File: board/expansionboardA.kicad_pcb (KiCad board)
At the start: 2 copper layers, 131 x 83.8 mm, 73 parts, among them J2 USB_A_Stacked, J3 HDMI_A, J4 USB_C_Receptacle, SW1 ESPPROG, U2 GPIO_U2, U3 SII164CTG64, U4 GPIO_U4, U5 ESP32-C6-WROOM-1-N8, U6 CS4344-CZZR, U7 MAX3421EEHJ+T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

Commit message: board update
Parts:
- added C3: 0.1uf, Capacitor_SMD:C_0603_1608Metric_Pad1.08x0.95mm_HandSolder, B.Cu at (79.5, 110.8)
- added SW2: ESPRESET, Button_Switch_SMD:SW_Tactile_SPST_NO_Straight_CK_PTS636Sx25SMTRLFS, B.Cu at (78.6, 117.3)
- SW1: moved to B.Cu
- moved SW1 0.30 mm to (71.8, 117.3)
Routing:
- net Net-(U5-EN): track 13.3 -> 73.3 mm, vias 0 -> 2
- net Net-(U5-IO9): vias 1 -> 2
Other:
- board text added: "RESET"
- board text removed: "D2"
- board text removed: "K4"
- board text removed: "L1"
- board text removed: "L3"
- board text removed: "M3"

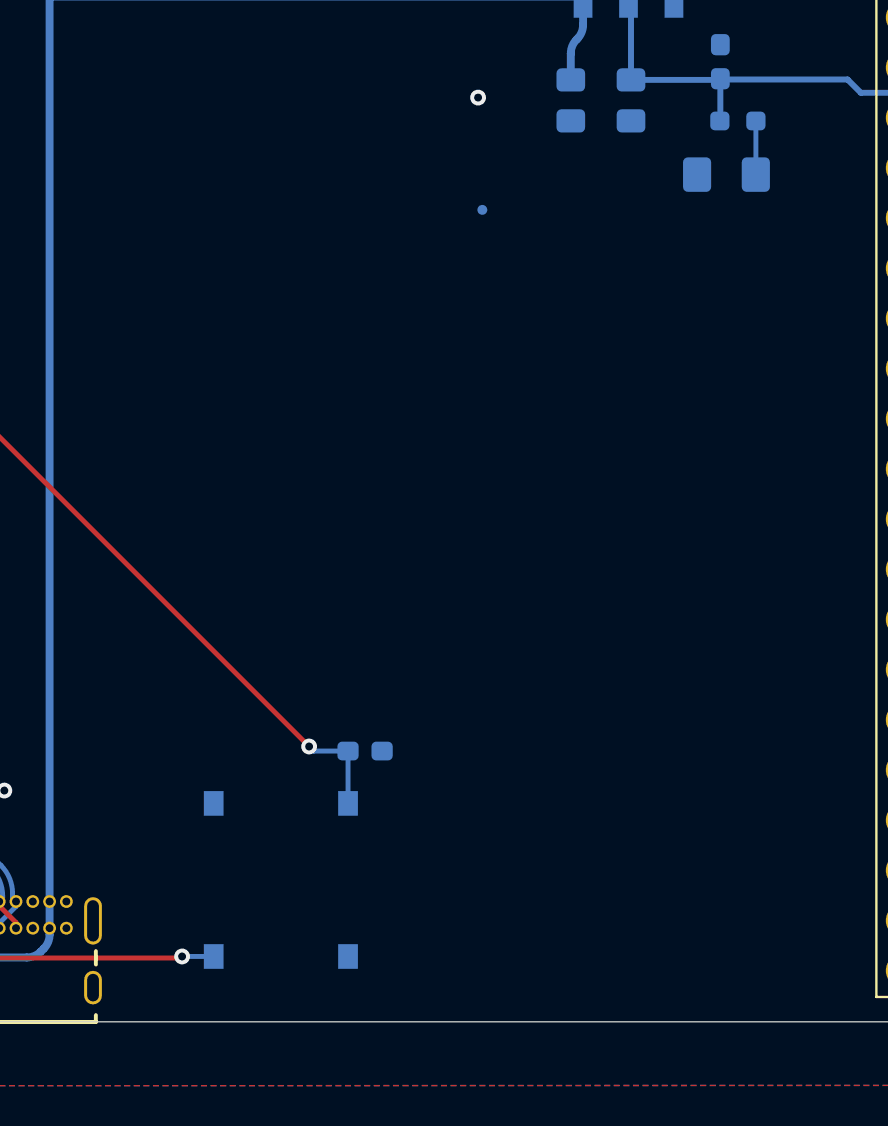
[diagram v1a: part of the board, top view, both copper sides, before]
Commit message: Some reboot/reset work Moved ADC to MIG as internal component Updated ROM startup sequence
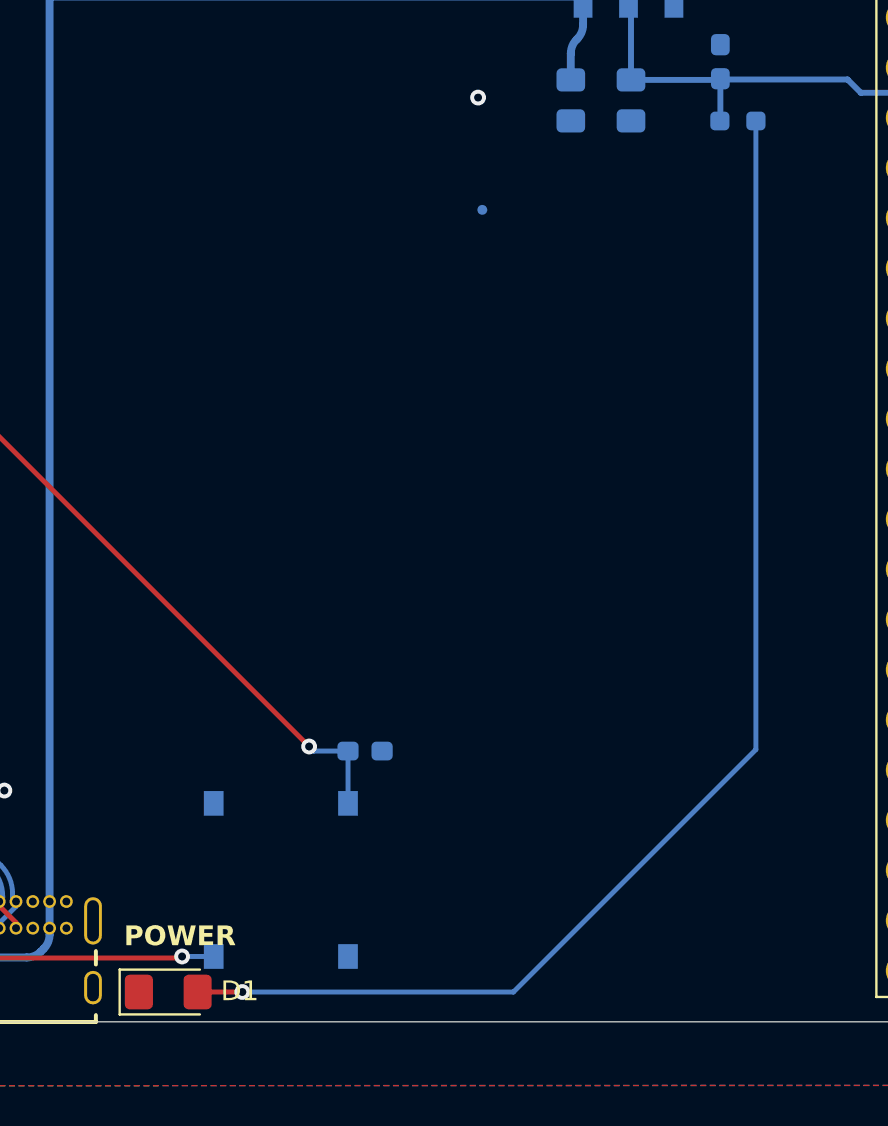
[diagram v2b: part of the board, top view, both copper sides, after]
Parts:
- D1: moved to F.Cu
- moved D1 50.1 mm to (69.5, 123.0)
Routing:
- net Net-(D1-A): track 2.72 -> 65.2 mm, vias 0 -> 1
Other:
- board text added: "ESP32 PROG & UART"
- board text removed: "ESP32 PROG"

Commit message: Board updates for version 2G Factory test ROM update
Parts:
- removed the REF** at (131.8, 96.2)
- removed the REF** at (121.8, 59.8)
- removed the REF** at (87.0, 49.0)
- removed the REF** at (62.2, 62.4)
- removed the REF** at (85.4, 83.4)
- removed the REF** at (148.2, 102.8)
- removed the REF** at (29.5, 66.2)
- removed the REF** at (35.8, 119.8)
- added U1: ESP32-S3, ESP32_S3:QFN56_7X7_EXP-L, B.Cu at (90.9, 104.6)
- moved D1 89.8 mm to (151.2, 85.8), turned to 90 degrees
- moved C3 13.1 mm to (67.2, 115.6), turned to 90 degrees
- moved SW2 5.54 mm to (73.1, 116.5), turned to 180 degrees
- moved SW1 4.14 mm to (73.1, 121.2), turned to 180 degrees
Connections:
- U3 pad 11: unconnected-(U3-MSEN-Pad11) -> MONITORSENSE
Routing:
- net 5V: track 183.8 -> 197.8 mm
- net Net-(D1-A): track 65.2 -> 53.9 mm
- net Net-(U5-IO9): track 41.6 -> 37.0 mm
- net GND: vias 35 -> 36
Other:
- board text added: "PROG UART"
- board text added: "tinysys issue 2G December 2024 Engin Cilasun"
- board text removed: "ESP32 PROG & UART"
- board text removed: "tinysys issue 2F April 2024 Engin Cilasun"

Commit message: New board files for future versions
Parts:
- removed C1: 1uf, Capacitor_SMD:C_0603_1608Metric_Pad1.08x0.95mm_HandSolder
- removed C15, C16: 18pf, Capacitor_SMD:C_0603_1608Metric_Pad1.08x0.95mm_HandSolder
- removed C18, C2, C3: 0.1uf, Capacitor_SMD:C_0603_1608Metric_Pad1.08x0.95mm_HandSolder
- removed C20: 4.7uf, Capacitor_SMD:CP_Elec_4x5.4
- removed J2: USB_A_Stacked, Connector_USB:USB_A_Molex_67643_Horizontal
- removed J4: USB_C_Receptacle, USB4085-GF-A_REVA4:GCT_USB4085-GF-A_REVA4
- removed R16, R17: 33Ohm, Resistor_SMD:R_0603_1608Metric_Pad0.98x0.95mm_HandSolder
- removed R25: 10KOhm, Resistor_SMD:R_0603_1608Metric_Pad0.98x0.95mm_HandSolder
- removed SW1: ESPPROG, Button_Switch_SMD:SW_Tactile_SPST_NO_Straight_CK_PTS636Sx25SMTRLFS
- removed SW2: ESPRESET, Button_Switch_SMD:SW_Tactile_SPST_NO_Straight_CK_PTS636Sx25SMTRLFS
- removed U5: ESP32-C6-WROOM-1-N8, ESP32_C6_WROOM:MOD28_ESP32-C6-WROOM-1_EXP
- removed U7: MAX3421EEHJ+T, MAX3421EEHJ_T:21-0110-C_90-0149-32L_MXM
- removed Y2: 403C35D12M00000, 403C35D12M00000:XTAL_403C35D12M00000
- added C4: 0.1uf, Capacitor_SMD:C_0603_1608Metric_Pad1.08x0.95mm_HandSolder, B.Cu at (75.4, 54.2)
- added C5: 0.1uf, Capacitor_SMD:C_0603_1608Metric_Pad1.08x0.95mm_HandSolder, B.Cu at (75.4, 57.3)
- added J1: USB_C_Receptacle, USB4085-GF-A_REVA4:GCT_USB4085-GF-A_REVA4, F.Cu at (23.8, 89.0)
- added R2: 10KOhm, Resistor_SMD:R_0603_1608Metric_Pad0.98x0.95mm_HandSolder, B.Cu at (75.5, 50.9)
- added SW3: ESPRESET, Button_Switch_SMD:SW_Tactile_SPST_NO_Straight_CK_PTS636Sx25SMTRLFS, B.Cu at (86.4, 47.4)
- added SW4: ESPPROG, Button_Switch_SMD:SW_Tactile_SPST_NO_Straight_CK_PTS636Sx25SMTRLFS, B.Cu at (86.5, 53.6)
- U1: value ESP32-S3 -> ESP32-S3-WROOM-1; footprint ESP32_S3:QFN56_7X7_EXP-L -> RF_Module:ESP32-S3-WROOM-1
- moved U1 64.1 mm to (62.0, 47.4)
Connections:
- U1 pad 1: unconnected-(U1-LNA_IN-Pad1) -> GND
- U1 pad 13: unconnected-(U1-GPIO8-Pad13) -> ESP2D_N
- U1 pad 14: unconnected-(U1-GPIO9-Pad14) -> ESP2D_P
- U1 pad 2: unconnected-(U1-VDD3P3-Pad2) -> REG3V3
- U1 pad 26: unconnected-(U1-GPIO20-Pad26) -> CPU_RESET
- U1 pad 27: unconnected-(U1-GPIO21-Pad27) -> Net-(U1-IO0)
- U1 pad 3: unconnected-(U1-VDD3P3-Pad3) -> Net-(U1-EN)
- U1 pad 36: unconnected-(U1-SPICLK_N-Pad36) -> RXD1
- U1 pad 37: unconnected-(U1-SPICLK_P-Pad37) -> TXD1
- U1 pad 4: unconnected-(U1-CHIP_PU-Pad4) -> S3_MISO
- U1 pad 40: unconnected-(U1-GPIO35-Pad40) -> GND
- U1 pad 41: unconnected-(U1-GPIO36-Pad41) -> GND
- U1 pad 5: unconnected-(U1-GPIO0-Pad5) -> S3_MOSI
- U1 pad 6: unconnected-(U1-GPIO1-Pad6) -> S3_MCLK
- U2 pad 10: RXD0 -> unconnected-(U2-Pin_10-Pad10)
- U2 pad 11: IO15 -> unconnected-(U2-Pin_11-Pad11)
- U2 pad 12: IO23 -> unconnected-(U2-Pin_12-Pad12)
- U2 pad 13: IO22 -> unconnected-(U2-Pin_13-Pad13)
- U2 pad 14: IO21 -> unconnected-(U2-Pin_14-Pad14)
- U2 pad 15: IO9 -> unconnected-(U2-Pin_15-Pad15)
- U2 pad 16: IO18 -> unconnected-(U2-Pin_16-Pad16)
- U2 pad 17: IO19 -> unconnected-(U2-Pin_17-Pad17)
- U2 pad 18: IO20 -> unconnected-(U2-Pin_18-Pad18)
- U2 pad 19: IO5 -> unconnected-(U2-Pin_19-Pad19)
- U2 pad 20: IO4 -> unconnected-(U2-Pin_20-Pad20)
- U2 pad 21: IO7 -> unconnected-(U2-Pin_21-Pad21)
- U2 pad 22: IO6 -> unconnected-(U2-Pin_22-Pad22)
- U2 pad 23: IO1 -> unconnected-(U2-Pin_23-Pad23)
- U2 pad 24: IO0 -> unconnected-(U2-Pin_24-Pad24)
- U2 pad 25: IO11 -> unconnected-(U2-Pin_25-Pad25)
- U2 pad 26: IO10 -> unconnected-(U2-Pin_26-Pad26)
- U2 pad 49: unconnected-(U2-Pin_49-Pad49) -> CPU_RESET
- U2 pad 51: unconnected-(U2-Pin_51-Pad51) -> S3_MCLK
- U2 pad 53: unconnected-(U2-Pin_53-Pad53) -> S3_MOSI
- U2 pad 55: unconnected-(U2-Pin_55-Pad55) -> S3_MISO
- U2 pad 57: unconnected-(U2-Pin_57-Pad57) -> RXD1
- U2 pad 59: unconnected-(U2-Pin_59-Pad59) -> TXD1
- U2 pad 9: TXD0 -> unconnected-(U2-Pin_9-Pad9)
- U4 pad 54: USBHINT -> unconnected-(U4-Pin_54-Pad54)
- U4 pad 55: USBHGPX -> unconnected-(U4-Pin_55-Pad55)
- U4 pad 56: USBHMOSI -> unconnected-(U4-Pin_56-Pad56)
- U4 pad 57: USBHMISO -> unconnected-(U4-Pin_57-Pad57)
- U4 pad 58: USBHCSN -> unconnected-(U4-Pin_58-Pad58)
- U4 pad 59: USBHSCLK -> unconnected-(U4-Pin_59-Pad59)
- U4 pad 60: USBHRES -> unconnected-(U4-Pin_60-Pad60)
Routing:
- net Net-(U5-EN): track 73.3 -> 0.00 mm, vias 2 -> 0
- net REG3V3: track 293.5 -> 228.3 mm, vias 4 -> 5
- net ESP2D_N: track 0.00 -> 64.6 mm
- net ESP2D_P: track 0.00 -> 64.4 mm
- net ESPD_N: track 49.5 -> 0.00 mm
- net ESPD_P: track 49.5 -> 0.00 mm
- net USBD1_N: track 44.6 -> 0.00 mm
- net USBD1_P: track 44.5 -> 0.00 mm
- net Net-(U5-IO9): track 37.0 -> 0.00 mm, vias 2 -> 0
- net Net-(U1-IO0): track 0.00 -> 33.1 mm, vias 0 -> 2
- net S3_MISO: track 0.00 -> 30.4 mm, vias 0 -> 1
- net S3_MOSI: track 0.00 -> 30.4 mm, vias 0 -> 1
- net S3_MCLK: track 0.00 -> 30.4 mm, vias 0 -> 1
- net IO2: track 28.2 -> 0.00 mm
- net TXD0: track 25.8 -> 0.00 mm
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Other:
- board text added: "DVI 1.0 OUT"
- board text added: "ESP32-S3-WROOM-1"
- board text added: "POWER & DATA"
- board text removed: "AA4"
- board text removed: "AA5"
- board text removed: "AA8"
- board text removed: "AB5"
- board text removed: "AB6"
- board text removed: "AB7"
- board text removed: "AB8"
- board text removed: "DVI 1.0"
- board text removed: "G20"
- board text removed: "H14"
- board text removed: "H17"
- board text removed: "H18"
- board text removed: "H20"
- board text removed: "H22"
- board text removed: "J14"
- board text removed: "J17"
- board text removed: "J19"
- board text removed: "J20"
- board text removed: "J21"
- board text removed: "J22"
- board text removed: "K13"
- board text removed: "K14"
- board text removed: "K17"
- board text removed: "K21"
- board text removed: "K22"
- board text removed: "L19"
- board text removed: "L20"
- board text removed: "PROG UART"

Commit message: Updates
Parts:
- removed C17: 1uf, Capacitor_SMD:C_0603_1608Metric_Pad1.08x0.95mm_HandSolder

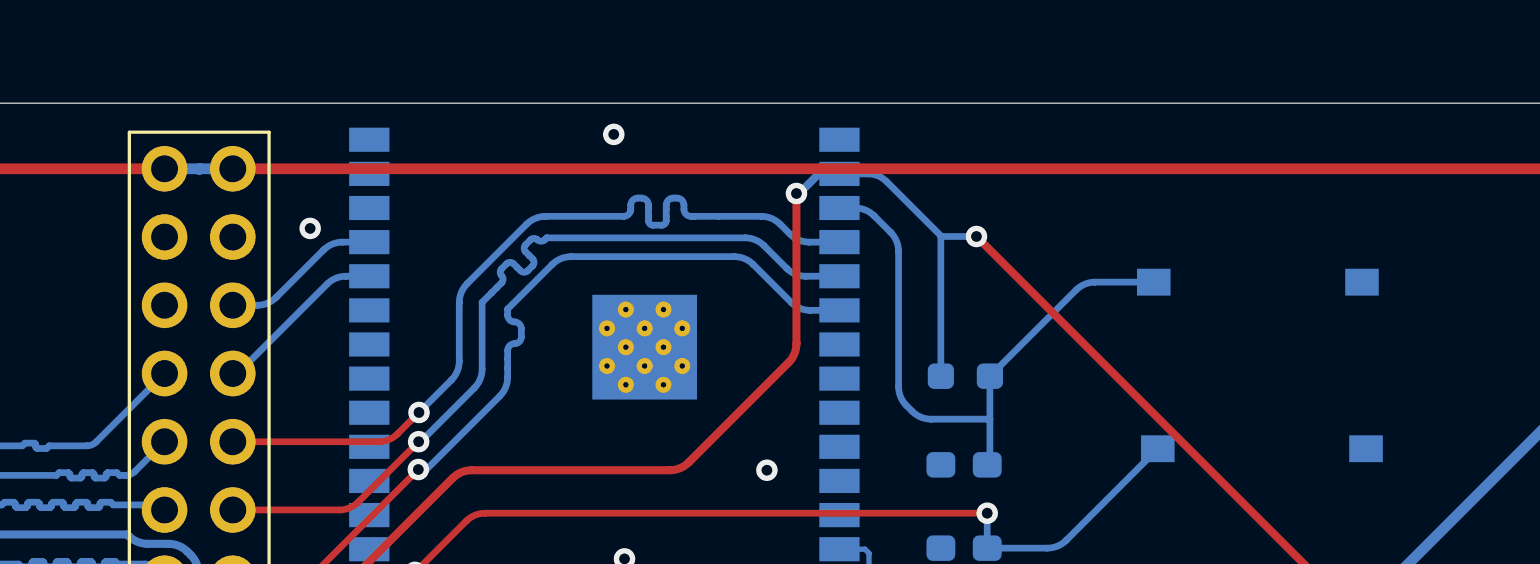
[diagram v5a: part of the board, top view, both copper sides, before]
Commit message: Updated board and hardware to reset ESP32 from the FPGA
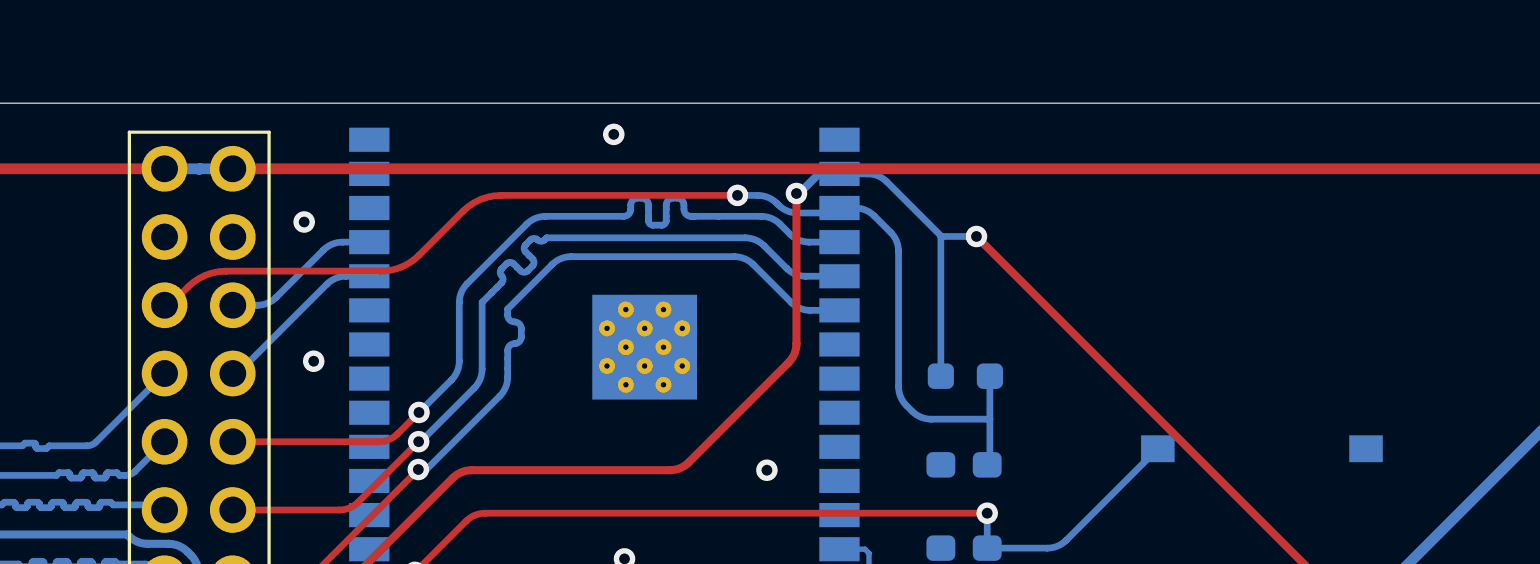
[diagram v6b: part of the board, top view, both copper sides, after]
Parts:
- removed SW3: ESPRESET, Button_Switch_SMD:SW_Tactile_SPST_NO_Straight_CK_PTS636Sx25SMTRLFS
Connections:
- C4 pad 1: Net-(U1-EN) -> ESP_RST
- R2 pad 1: Net-(U1-EN) -> ESP_RST
- U1 pad 3: Net-(U1-EN) -> ESP_RST
- U2 pad 60: unconnected-(U2-Pin_60-Pad60) -> ESP_RST
- U2 pad 7: IO2 -> unconnected-(U2-Pin_7-Pad7)
- U2 pad 8: IO3 -> unconnected-(U2-Pin_8-Pad8)
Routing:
- net ESP_RST: track 0.00 -> 42.2 mm, vias 0 -> 1
- net Net-(U1-EN): track 22.9 -> 0.00 mm
- net GND: vias 33 -> 34
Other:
- board text removed: "RESET"
